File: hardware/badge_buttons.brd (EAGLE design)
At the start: 92.2 x 63.6 mm, 7 parts

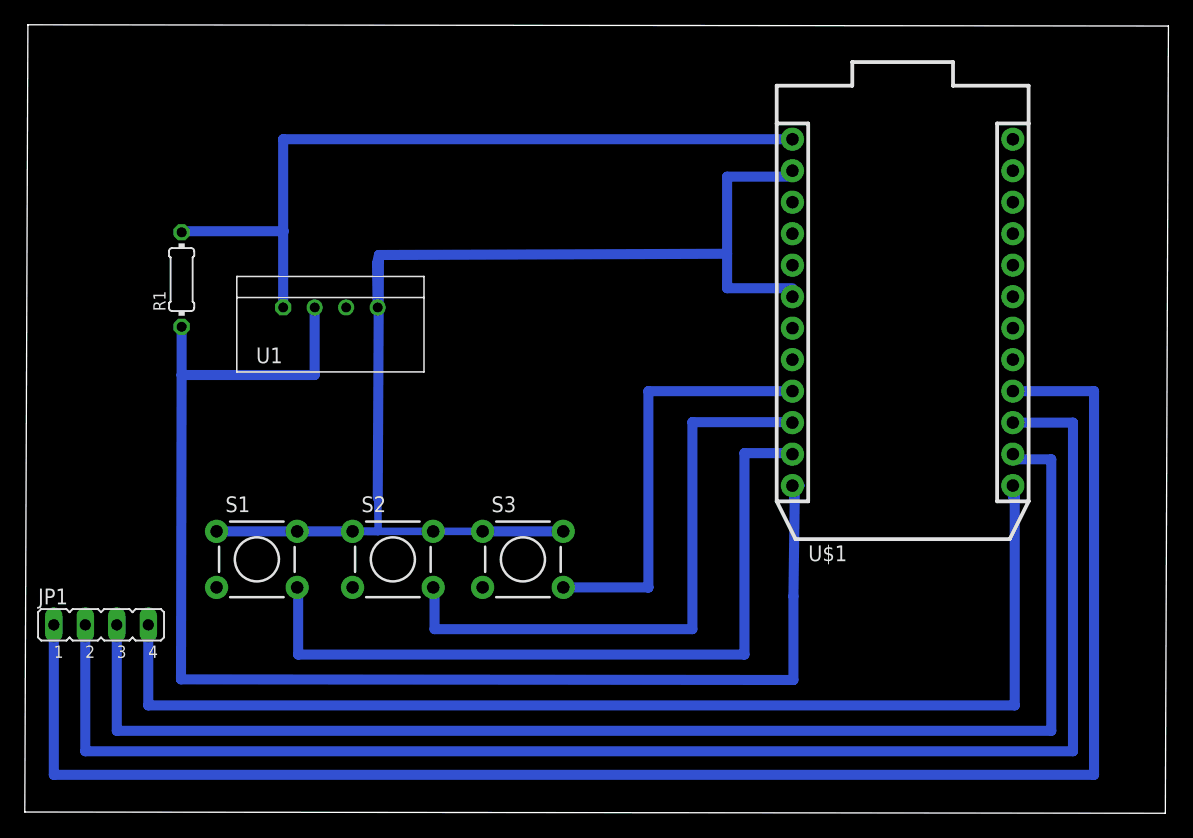
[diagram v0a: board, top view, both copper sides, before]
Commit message: fattened pads
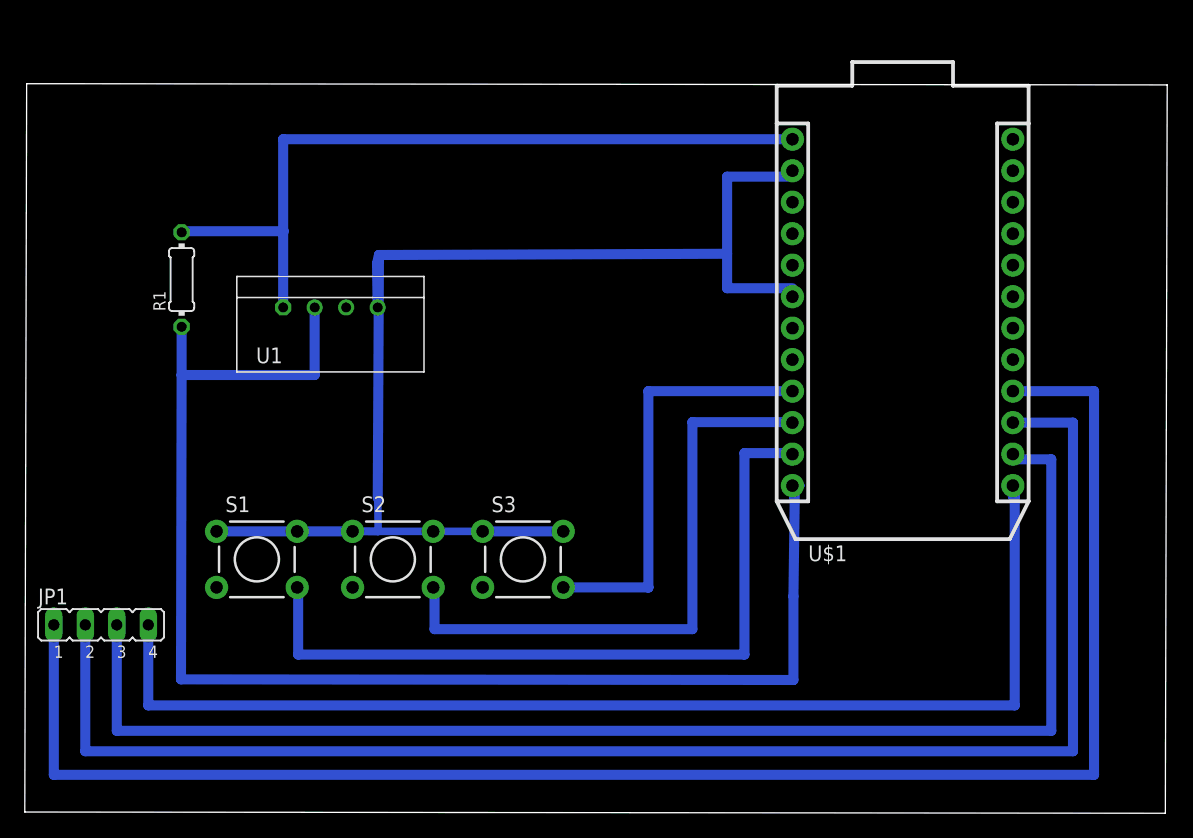
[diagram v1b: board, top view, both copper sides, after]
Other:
- board size 92.2 x 63.6 mm -> 92.2 x 58.9 mm
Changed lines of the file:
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@@
 <plain>
 <wire x1="3.35" y1="4.75" x2="95.35" y2="4.65" width="0" layer="20"/>
-<wire x1="95.35" y1="4.65" x2="95.6" y2="68.15" width="0" layer="20"/>
-<wire x1="95.6" y1="68.15" x2="3.6" y2="68.25" width="0" layer="20"/>
-<wire x1="3.6" y1="68.25" x2="3.35" y2="4.75" width="0" layer="20"/>
+<wire x1="95.35" y1="4.65" x2="95.5" y2="63.4" width="0" layer="20"/>
+<wire x1="95.5" y1="63.4" x2="3.5" y2="63.5" width="0" layer="20"/>
+<wire x1="3.5" y1="63.5" x2="3.35" y2="4.75" width="0" layer="20"/>
+<rectangle x1="63.15" y1="58.15" x2="67.35" y2="59.85" layer="17"/>
+<rectangle x1="63.1" y1="55.65" x2="67.3" y2="57.35" layer="17"/>
+<rectangle x1="63.1" y1="53.1" x2="67.3" y2="54.8" layer="17"/>
+<rectangle x1="63.1" y1="50.55" x2="67.3" y2="52.25" layer="17"/>
+<rectangle x1="63.05" y1="48.05" x2="67.25" y2="49.75" layer="17"/>
+<rectangle x1="63.05" y1="45.5" x2="67.25" y2="47.2" layer="17"/>
+<rectangle x1="63.1" y1="42.9" x2="67.3" y2="44.6" layer="17"/>
+<rectangle x1="63.05" y1="40.4" x2="67.25" y2="42.1" layer="17"/>
+<rectangle x1="63.05" y1="37.85" x2="67.25" y2="39.55" layer="17"/>
+<rectangle x1="63.05" y1="35.3" x2="67.25" y2="37" layer="17"/>
+<rectangle x1="63" y1="32.8" x2="67.2" y2="34.5" layer="17"/>
+<rectangle x1="63" y1="30.25" x2="67.2" y2="31.95" layer="17"/>
+<rectangle x1="80.85" y1="58.05" x2="85.05" y2="59.75" layer="17"/>
+<rectangle x1="80.8" y1="55.55" x2="85" y2="57.25" layer="17"/>
+<rectangle x1="80.8" y1="53" x2="85" y2="54.7" layer="17"/>
+<rectangle x1="80.8" y1="50.45" x2="85" y2="52.15" layer="17"/>
+<rectangle x1="80.75" y1="47.95" x2="84.95" y2="49.65" layer="17"/>
+<rectangle x1="80.75" y1="45.4" x2="84.95" y2="47.1" layer="17"/>
+<rectangle x1="80.8" y1="42.8" x2="85" y2="44.5" layer="17"/>
+<rectangle x1="80.75" y1="40.3" x2="84.95" y2="42" layer="17"/>
+<rectangle x1="80.75" y1="37.75" x2="84.95" y2="39.45" layer="17"/>
+<rectangle x1="80.75" y1="35.2" x2="84.95" y2="36.9" layer="17"/>
+<rectangle x1="80.7" y1="32.7" x2="84.9" y2="34.4" layer="17"/>
+<rectangle x1="80.7" y1="30.15" x2="84.9" y2="31.85" layer="17"/>
+<rectangle x1="18.1" y1="25.85" x2="19.55" y2="28.85" layer="17"/>
+<rectangle x1="18.4" y1="28.2" x2="19.15" y2="28.35" layer="17"/>
+<rectangle x1="18" y1="21.4" x2="19.45" y2="24.4" layer="17"/>
+<rectangle x1="24.65" y1="25.85" x2="26.1" y2="28.85" layer="17"/>
+<rectangle x1="24.55" y1="21.4" x2="26" y2="24.4" layer="17"/>
+<rectangle x1="29.1" y1="25.95" x2="30.55" y2="28.95" layer="17"/>
+<rectangle x1="29.05" y1="21.45" x2="30.5" y2="24.45" layer="17"/>
+<rectangle x1="35.65" y1="25.9" x2="37.1" y2="28.9" layer="17"/>
+<rectangle x1="35.7" y1="21.45" x2="37.15" y2="24.45" layer="17"/>
+<rectangle x1="39.4" y1="26.05" x2="40.85" y2="29.05" layer="17"/>
+<rectangle x1="39.45" y1="21.45" x2="40.9" y2="24.45" layer="17"/>
+<rectangle x1="46.05" y1="25.95" x2="47.5" y2="28.95" layer="17"/>
+<rectangle x1="46.1" y1="21.4" x2="47.55" y2="24.4" layer="17"/>
+<rectangle x1="23.5" y1="43.9" x2="24.95" y2="46.9" layer="17"/>
+<rectangle x1="25.95" y1="43.95" x2="27.4" y2="46.95" layer="17"/>
+<rectangle x1="28.7" y1="44.05" x2="30.15" y2="47.05" layer="17"/>
+<rectangle x1="31" y1="43.95" x2="32.45" y2="46.95" layer="17"/>
+<rectangle x1="15.35" y1="50.55" x2="16.8" y2="53.55" layer="17"/>
+<rectangle x1="15.25" y1="41.7" x2="16.7" y2="44.7" layer="17"/>
 </plain>
 <attributes>

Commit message: power hogging
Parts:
- added R2: (no value), resistor:0204/7
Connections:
- net N$1: now also S3.3
- net N$2: now also S2.3
- net N$3: now also S1.3
- net N$4: now also R2.1
- net N$5: now also R2.2
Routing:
- net N$2: track 49.1 -> 55.9 mm
- net N$3: track 61.7 -> 68.2 mm
- net N$1: track 34.8 -> 41.3 mm
- net N$4: track 105.3 -> 106.4 mm
- net N$5: track 63.0 -> 63.6 mm
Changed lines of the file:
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@@
 <rectangle x1="15.35" y1="50.55" x2="16.8" y2="53.55" layer="17"/>
 <rectangle x1="15.25" y1="41.7" x2="16.7" y2="44.7" layer="17"/>
+<rectangle x1="38.95" y1="58.05" x2="41.3" y2="60.15" layer="17"/>
+<rectangle x1="38.55" y1="47.95" x2="41.65" y2="51.5" layer="17"/>
 </plain>
 <attributes>
@@
 <element name="R1" library="resistor" library_urn="urn:adsk.eagle:library:348" package="0204/7" package3d_urn="urn:adsk.eagle:package:25945/1" value="" x="16" y="47.7" rot="R90"/>
 <element name="JP1" library="jumper" library_urn="urn:adsk.eagle:library:252" package="JP4" package3d_urn="urn:adsk.eagle:package:15463/1" value="" x="9.5" y="19.85"/>
+<element name="R2" library="resistor" library_urn="urn:adsk.eagle:library:348" package="0204/7" package3d_urn="urn:adsk.eagle:package:25945/1" value="" x="40.05" y="54.6" rot="R90"/>
 </elements>
 <signals>
@@
 <wire x1="65.27" y1="38.7" x2="65" y2="38.97" width="0.3048" layer="16"/>
 <wire x1="65" y1="38.97" x2="65" y2="39" width="0.3048" layer="16"/>
-<wire x1="46.7812" y1="22.8694" x2="53.65" y2="22.8694" width="0.8128" layer="16"/>
+<wire x1="46.7812" y1="22.8694" x2="47.15" y2="22.8694" width="0.8128" layer="16"/>
+<wire x1="47.15" y1="22.8694" x2="53.65" y2="22.8694" width="0.8128" layer="16"/>
 <wire x1="53.65" y1="22.8694" x2="53.65" y2="22.85" width="0.8128" layer="16"/>
 <wire x1="53.65" y1="22.8694" x2="53.65" y2="38.7" width="0.8128" layer="16"/>
 <wire x1="53.65" y1="38.7" x2="65.27" y2="38.7" width="0.8128" layer="16"/>
+<contactref element="S3" pad="3"/>
+<wire x1="40.2788" y1="22.8694" x2="46.7812" y2="22.8694" width="0.8128" layer="16"/>
 </signal>
 <signal name="N$2">
@@
 <contactref element="U$1" pad="10"/>
 <wire x1="36.2912" y1="22.8694" x2="36.4" y2="22.8694" width="0.8128" layer="16"/>
-<wire x1="36.4" y1="22.8694" x2="36.4" y2="19.5" width="0.8128" layer="16"/>
+<wire x1="36.4" y1="22.8694" x2="36.4" y2="22.5" width="0.8128" layer="16"/>
+<wire x1="36.4" y1="22.5" x2="36.4" y2="19.5" width="0.8128" layer="16"/>
 <wire x1="36.4" y1="19.5" x2="57.2" y2="19.5" width="0.8128" layer="16"/>
 <wire x1="57.2" y1="19.5" x2="57.2" y2="36.2" width="0.8128" layer="16"/>
 <wire x1="57.2" y1="36.2" x2="65.27" y2="36.2" width="0.8128" layer="16"/>
 <wire x1="65.27" y1="36.2" x2="65.27" y2="36.16" width="0.8128" layer="16"/>
+<contactref element="S2" pad="3"/>
+<wire x1="29.7888" y1="22.8694" x2="30.1582" y2="22.5" width="0.8128" layer="16"/>
+<wire x1="30.1582" y1="22.5" x2="36.4" y2="22.5" width="0.8128" layer="16"/>
 </signal>
 <signal name="N$3">
@@
 <wire x1="61.4" y1="33.7" x2="65.27" y2="33.7" width="0.8128" layer="16"/>
 <wire x1="65.27" y1="33.7" x2="65.27" y2="33.62" width="0.8128" layer="16"/>
+<contactref element="S1" pad="3"/>
+<wire x1="18.8188" y1="22.8694" x2="25.3212" y2="22.8694" width="0.8128" layer="16"/>
 </signal>
 <signal name="N$4">
@@
 <wire x1="31.85305" y1="27.371971875" x2="30" y2="27.3906" width="0.6096" layer="16"/>
 <wire x1="60" y1="49.78" x2="55.0003125" y2="49.76219375" width="0.8128" layer="16"/>
-<wire x1="55.0003125" y1="49.76219375" x2="31.92" y2="49.68" width="0.8128" layer="16"/>
+<wire x1="55.0003125" y1="49.76219375" x2="40.1012125" y2="49.709134375" width="0.8128" layer="16"/>
+<wire x1="40.1012125" y1="49.709134375" x2="31.92" y2="49.68" width="0.8128" layer="16"/>
 <wire x1="65.27" y1="46.32" x2="65.27" y2="47" width="0.508" layer="16"/>
 <wire x1="60" y1="47" x2="65.27" y2="47" width="0.8128" layer="16"/>
-<wire x1="60" y1="49.78" x2="60" y2="47.45" width="0.8128" layer="16"/>
+<wire x1="60" y1="49.78" x2="60" y2="47" width="0.8128" layer="16"/>
 <wire x1="65.27" y1="56.48" x2="65.27" y2="56" width="0.6096" layer="16"/>
 <wire x1="65.27" y1="56" x2="60" y2="56" width="0.8128" layer="16"/>
 <wire x1="60" y1="56" x2="60" y2="49.78" width="0.8128" layer="16"/>
 <wire x1="18.75" y1="27.3906" x2="18.8188" y2="27.3906" width="0.8128" layer="1"/>
-<wire x1="60" y1="47.45" x2="60" y2="47" width="0.8128" layer="16"/>
+<contactref element="R2" pad="1"/>
+<wire x1="40.05" y1="50.79" x2="40.05" y2="49.760346875" width="0.8128" layer="16"/>
+<wire x1="40.05" y1="49.760346875" x2="40.1012125" y2="49.709134375" width="0.8128" layer="16"/>
 </signal>
 <signal name="N$5">
@@
 <wire x1="16" y1="51.6" x2="16" y2="51.51" width="0.8128" layer="16"/>
 <wire x1="24.19" y1="51.6" x2="24.19" y2="59.02" width="0.8128" layer="16"/>
-<wire x1="24.19" y1="59.02" x2="65.27" y2="59.02" width="0.8128" layer="16"/>
+<wire x1="24.19" y1="59.02" x2="39.95" y2="59.02" width="0.8128" layer="16"/>
+<contactref element="R2" pad="2"/>
+<wire x1="39.95" y1="59.02" x2="65.27" y2="59.02" width="0.8128" layer="16"/>
+<wire x1="40.05" y1="58.41" x2="40.05" y2="58.92" width="0.8128" layer="16"/>
+<wire x1="40.05" y1="58.92" x2="39.95" y2="59.02" width="0.8128" layer="16"/>
 </signal>
 <signal name="N$6">
